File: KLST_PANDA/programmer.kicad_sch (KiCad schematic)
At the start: 8 parts, among them J1 ARM_JTAG_SWD(STDC14), J1 TC2070-IDC-NL

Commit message: started spec'ing components
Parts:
- J1: JLCPCB (none) -> DNF; JLCPCB Part # DNF -> (none)
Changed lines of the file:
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@@
       (effects (font (size 1.27 1.27)) hide)
     )
-    (property "JLCPCB Part #" "DNF" (at 31.75 46.99 0)
+    (property "JLCPCB Part #" "" (at 31.75 46.99 0)
+      (effects (font (size 1.27 1.27)) hide)
+    )
+    (property "JLCPCB" "DNF" (at 31.75 46.99 0)
       (effects (font (size 1.27 1.27)) hide)
     )
@@
       (effects (font (size 1.27 1.27)) hide)
     )
-    (property "JLCPCB Part #" "DNF" (at 100.965 46.99 0)
+    (property "JLCPCB Part #" "" (at 100.965 46.99 0)
       (effects (font (size 1.27 1.27)) hide)
     )
+    (property "JLCPCB" "DNF" (at 100.965 46.99 0)
+      (effects (font (size 1.27 1.27)) hide)
+    )

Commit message: assigned footprints
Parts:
- R53, R54, R55, R56, R57, R58: footprint (none) -> Resistor_SMD:R_0402_1005Metric; JLCPCB (none) -> C114765
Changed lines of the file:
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@@
       (effects (font (size 1.27 1.27)))
     )
-    (property "Footprint" "" (at 191.135 36.83 0)
+    (property "Footprint" "Resistor_SMD:R_0402_1005Metric" (at 191.135 36.83 0)
       (effects (font (size 1.27 1.27)) hide)
     )
     (property "Datasheet" "~" (at 191.135 36.83 0)
+      (effects (font (size 1.27 1.27)) hide)
+    )
+    (property "Description" "62.5mW" (at 191.135 36.83 0)
+      (effects (font (size 1.27 1.27)) hide)
+    )
+    (property "JLCPCB" "C114765" (at 191.135 36.83 0)
       (effects (font (size 1.27 1.27)) hide)
     )
@@
       (effects (font (size 1.27 1.27)))
     )
-    (property "Footprint" "" (at 191.135 55.88 0)
+    (property "Footprint" "Resistor_SMD:R_0402_1005Metric" (at 191.135 55.88 0)
       (effects (font (size 1.27 1.27)) hide)
     )
     (property "Datasheet" "~" (at 191.135 55.88 0)
+      (effects (font (size 1.27 1.27)) hide)
+    )
+    (property "Description" "62.5mW" (at 191.135 55.88 0)
+      (effects (font (size 1.27 1.27)) hide)
+    )
+    (property "JLCPCB" "C114765" (at 191.135 55.88 0)
       (effects (font (size 1.27 1.27)) hide)
     )
@@
       (effects (font (size 1.27 1.27)))
     )
-    (property "Footprint" "" (at 191.135 43.18 0)
+    (property "Footprint" "Resistor_SMD:R_0402_1005Metric" (at 191.135 43.18 0)
       (effects (font (size 1.27 1.27)) hide)
     )
@@
       (effects (font (size 1.27 1.27)) hide)
     )
+    (property "Description" "62.5mW" (at 191.135 43.18 0)
+      (effects (font (size 1.27 1.27)) hide)
+    )
+    (property "JLCPCB" "C114765" (at 191.135 43.18 0)
+      (effects (font (size 1.27 1.27)) hide)
+    )
     (pin "1")
     (pin "2")
@@
       (effects (font (size 1.27 1.27)))
     )
-    (property "Footprint" "" (at 191.135 49.53 0)
+    (property "Footprint" "Resistor_SMD:R_0402_1005Metric" (at 191.135 49.53 0)
       (effects (font (size 1.27 1.27)) hide)
     )
     (property "Datasheet" "~" (at 191.135 49.53 0)
+      (effects (font (size 1.27 1.27)) hide)
+    )
+    (property "Description" "62.5mW" (at 191.135 49.53 0)
+      (effects (font (size 1.27 1.27)) hide)
+    )
+    (property "JLCPCB" "C114765" (at 191.135 49.53 0)
       (effects (font (size 1.27 1.27)) hide)
     )
@@
       (effects (font (size 1.27 1.27)))
     )
-    (property "Footprint" "" (at 191.135 62.23 0)
+    (property "Footprint" "Resistor_SMD:R_0402_1005Metric" (at 191.135 62.23 0)
       (effects (font (size 1.27 1.27)) hide)
     )
     (property "Datasheet" "~" (at 191.135 62.23 0)
+      (effects (font (size 1.27 1.27)) hide)
+    )
+    (property "Description" "62.5mW" (at 191.135 62.23 0)
+      (effects (font (size 1.27 1.27)) hide)
+    )
+    (property "JLCPCB" "C114765" (at 191.135 62.23 0)
       (effects (font (size 1.27 1.27)) hide)
     )
@@
       (effects (font (size 1.27 1.27)))
     )
-    (property "Footprint" "" (at 191.135 30.48 0)
+    (property "Footprint" "Resistor_SMD:R_0402_1005Metric" (at 191.135 30.48 0)
       (effects (font (size 1.27 1.27)) hide)
     )
@@
       (effects (font (size 1.27 1.27)) hide)
     )
+    (property "Description" "62.5mW" (at 191.135 30.48 0)
+      (effects (font (size 1.27 1.27)) hide)
+    )
+    (property "JLCPCB" "C114765" (at 191.135 30.48 0)
+      (effects (font (size 1.27 1.27)) hide)
+    )

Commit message: cleaned up footprint assignment
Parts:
- J1: MFR.Part # DNF -> (none)
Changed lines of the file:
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@@
-      (effects (font (size 1.27 1.27)) hide)
-    )
-    (property "LCSC Part #" "" (at 31.75 46.99 0)
-      (effects (font (size 1.27 1.27)) hide)
-    )
-    (property "MFR.Part #" "DNF" (at 31.75 46.99 0)
-      (effects (font (size 1.27 1.27)) hide)
-    )
-    (property "JLCPCB Part #" "" (at 31.75 46.99 0)
       (effects (font (size 1.27 1.27)) hide)
     )
@@
       (effects (font (size 1.27 1.27)) hide)
     )
-    (property "LCSC Part #" "" (at 100.965 46.99 0)
-      (effects (font (size 1.27 1.27)) hide)
-    )
-    (property "MFR.Part #" "DNF" (at 100.965 46.99 0)
-      (effects (font (size 1.27 1.27)) hide)
-    )
-    (property "JLCPCB Part #" "" (at 100.965 46.99 0)
-      (effects (font (size 1.27 1.27)) hide)
-    )

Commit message: routed some components
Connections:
- net NRST: no longer J1.12 (~{RST}), J1.12 (~{RST}), R53.1
- new net RST: J1.12 (~{RST}), J1.12 (~{RST}), R53.1
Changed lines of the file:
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@@
     (effects (font (size 1.27 1.27)) (justify left bottom))
   )
-  (label "NRST" (at 44.45 34.29 0) (fields_autoplaced)
+  (label "RST" (at 44.45 34.29 0) (fields_autoplaced)
     (effects (font (size 1.27 1.27)) (justify left bottom))
   )
@@
     (effects (font (size 1.27 1.27)) (justify left bottom))
   )
+  (label "RST" (at 186.055 30.48 180) (fields_autoplaced)
+    (effects (font (size 1.27 1.27)) (justify right bottom))
+  )
   (label "SWD_OUT" (at 113.665 44.45 0) (fields_autoplaced)
     (effects (font (size 1.27 1.27)) (justify left bottom))
   )
-  (label "NRST" (at 186.055 30.48 180) (fields_autoplaced)
-    (effects (font (size 1.27 1.27)) (justify right bottom))
+  (label "SERIAL_TX" (at 113.665 59.69 0) (fields_autoplaced)
+    (effects (font (size 1.27 1.27)) (justify left bottom))
   )
-  (label "SERIAL_TX" (at 113.665 59.69 0) (fields_autoplaced)
+  (label "RST" (at 113.665 34.29 0) (fields_autoplaced)
     (effects (font (size 1.27 1.27)) (justify left bottom))
   )
@@
     (effects (font (size 1.27 1.27)) (justify right bottom))
   )
-  (label "NRST" (at 113.665 34.29 0) (fields_autoplaced)
-    (effects (font (size 1.27 1.27)) (justify left bottom))
-  )
   (label "SWD_CLK" (at 44.45 39.37 0) (fields_autoplaced)

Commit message: added ( maybe fit ) Samtec FTSH-107-01-F-DV-K for programmer
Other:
- note added: "@TODO( maybe fit Samtec FTSH-107-01-F-DV-K for assembly )"
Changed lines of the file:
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@@
+    (effects (font (size 1.27 1.27)) (justify left bottom))
+  )
+  (text "@TODO( maybe fit Samtec FTSH-107-01-F-DV-K for assembly )"
+    (at 15.875 78.105 0)
     (effects (font (size 1.27 1.27)) (justify left bottom))
   )

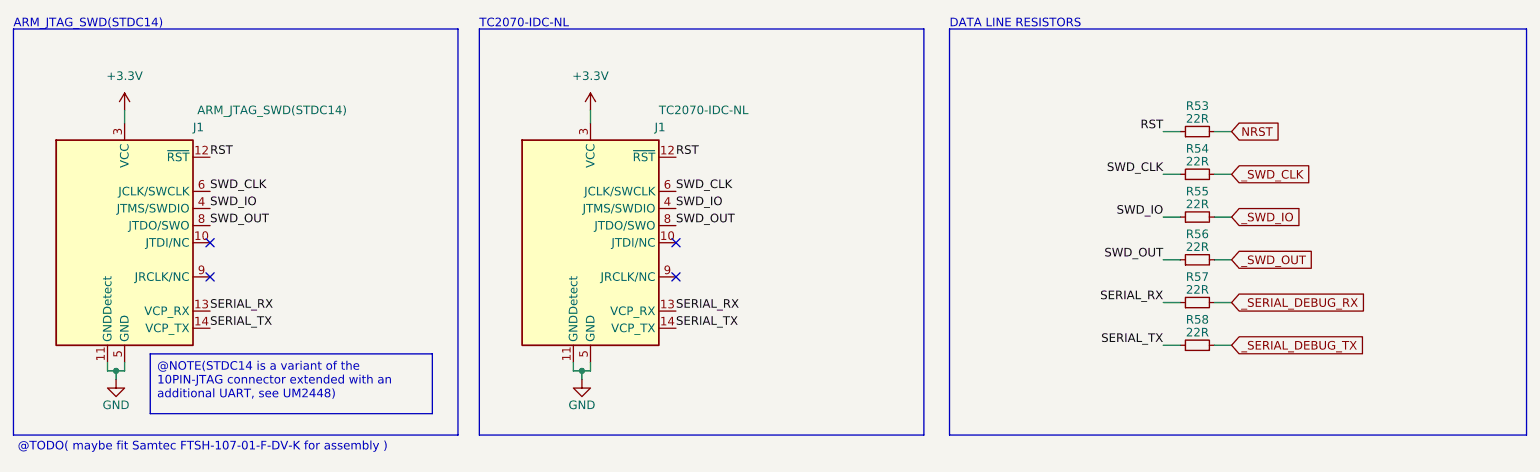
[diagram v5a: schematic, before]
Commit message: added resistor and capacitor, cleaned up TODOs
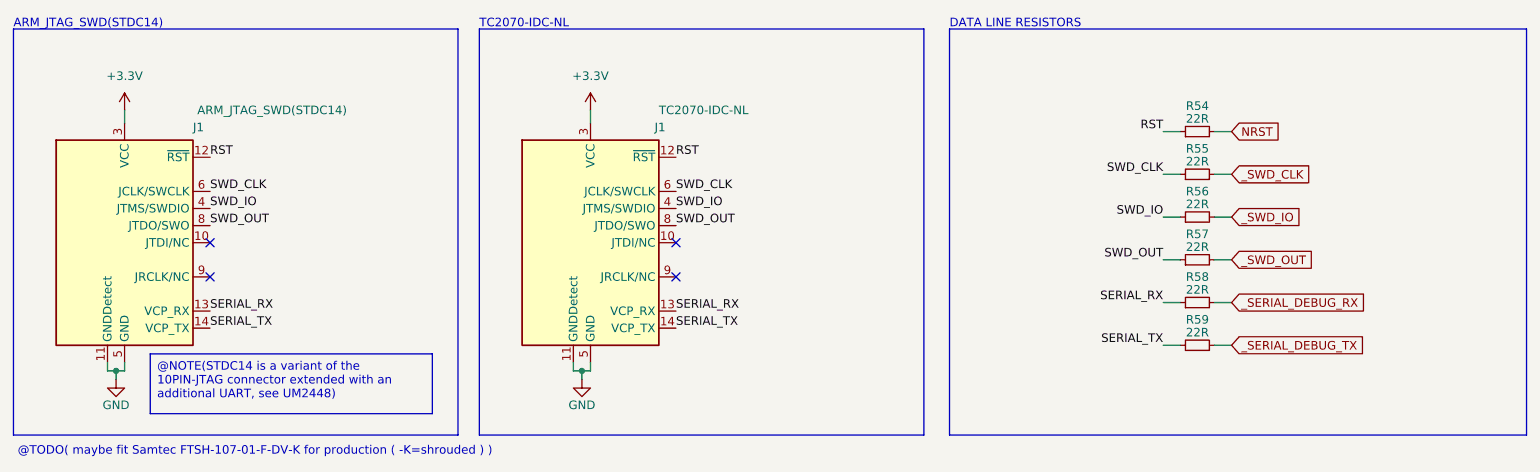
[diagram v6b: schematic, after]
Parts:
- J1: JLCPCB DNF -> C2881912
- renumbered R53 to R54, R54 to R55, R55 to R56, R56 to R57, R57 to R58, R58 to R59
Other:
- note added: "@TODO( maybe fit Samtec FTSH-107-01-F-DV-K for production ( -K=shrouded ) )"
- note removed: "@TODO( maybe fit Samtec FTSH-107-01-F-DV-K for assembly )"
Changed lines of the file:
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@@
     (effects (font (size 1.27 1.27)) (justify left bottom))
   )
-  (text "@TODO( maybe fit Samtec FTSH-107-01-F-DV-K for assembly )"
-    (at 15.875 78.105 0)
+  (text "@TODO( maybe fit Samtec FTSH-107-01-F-DV-K for production ( -K=shrouded ) )"
+    (at 15.875 78.74 0)
     (effects (font (size 1.27 1.27)) (justify left bottom))
   )
@@
   (symbol (lib_id "Device:R_Small") (at 191.135 36.83 90) (unit 1)
     (in_bom yes) (on_board yes) (dnp no)
-    (property "Reference" "R54" (at 191.135 33.02 90)
+    (property "Reference" "R55" (at 191.135 33.02 90)
       (effects (font (size 1.27 1.27)))
     )
@@
       (project "KLST_PANDA"
         (path "/b4513875-4c57-4720-bcc5-43ead67fe18f/2ad43130-8b99-4527-817e-e6414020b242"
-          (reference "R54") (unit 1)
+          (reference "R55") (unit 1)
         )
       )
@@
         )
         (path "/b4513875-4c57-4720-bcc5-43ead67fe18f/2ad43130-8b99-4527-817e-e6414020b242"
-          (reference "#PWR086") (unit 1)
+          (reference "#PWR088") (unit 1)
         )
       )
@@
   (symbol (lib_id "Device:R_Small") (at 191.135 55.88 90) (unit 1)
     (in_bom yes) (on_board yes) (dnp no)
-    (property "Reference" "R57" (at 191.135 52.07 90)
+    (property "Reference" "R58" (at 191.135 52.07 90)
       (effects (font (size 1.27 1.27)))
     )
@@
       (project "KLST_PANDA"
         (path "/b4513875-4c57-4720-bcc5-43ead67fe18f/2ad43130-8b99-4527-817e-e6414020b242"
-          (reference "R57") (unit 1)
+          (reference "R58") (unit 1)
         )
       )
@@
       (effects (font (size 1.27 1.27)) hide)
     )
-    (property "JLCPCB" "DNF" (at 31.75 46.99 0)
+    (property "JLCPCB" "C2881912" (at 31.75 46.99 0)
       (effects (font (size 1.27 1.27)) hide)
     )
@@
         )
         (path "/b4513875-4c57-4720-bcc5-43ead67fe18f/2ad43130-8b99-4527-817e-e6414020b242"
-          (reference "#PWR087") (unit 1)
+          (reference "#PWR089") (unit 1)
         )
       )
@@
   (symbol (lib_id "Device:R_Small") (at 191.135 43.18 90) (unit 1)
     (in_bom yes) (on_board yes) (dnp no)
-    (property "Reference" "R55" (at 191.135 39.37 90)
+    (property "Reference" "R56" (at 191.135 39.37 90)
       (effects (font (size 1.27 1.27)))
     )
@@
       (project "KLST_PANDA"
         (path "/b4513875-4c57-4720-bcc5-43ead67fe18f/2ad43130-8b99-4527-817e-e6414020b242"
-          (reference "R55") (unit 1)
+          (reference "R56") (unit 1)
         )
       )
@@
   (symbol (lib_id "Device:R_Small") (at 191.135 49.53 90) (unit 1)
     (in_bom yes) (on_board yes) (dnp no)
-    (property "Reference" "R56" (at 191.135 45.72 90)
+    (property "Reference" "R57" (at 191.135 45.72 90)
       (effects (font (size 1.27 1.27)))
     )
@@
       (project "KLST_PANDA"
         (path "/b4513875-4c57-4720-bcc5-43ead67fe18f/2ad43130-8b99-4527-817e-e6414020b242"
-          (reference "R56") (unit 1)
+          (reference "R57") (unit 1)
         )
       )
@@
         )
         (path "/b4513875-4c57-4720-bcc5-43ead67fe18f/2ad43130-8b99-4527-817e-e6414020b242"
-          (reference "#PWR085") (unit 1)
+          (reference "#PWR087") (unit 1)
         )
       )
@@
   (symbol (lib_id "Device:R_Small") (at 191.135 62.23 90) (unit 1)
     (in_bom yes) (on_board yes) (dnp no)
-    (property "Reference" "R58" (at 191.135 58.42 90)
+    (property "Reference" "R59" (at 191.135 58.42 90)
       (effects (font (size 1.27 1.27)))
     )
@@
       (project "KLST_PANDA"
         (path "/b4513875-4c57-4720-bcc5-43ead67fe18f/2ad43130-8b99-4527-817e-e6414020b242"
-          (reference "R58") (unit 1)
+          (reference "R59") (unit 1)
         )
       )
@@
   (symbol (lib_id "Device:R_Small") (at 191.135 30.48 90) (unit 1)
     (in_bom yes) (on_board yes) (dnp no)
-    (property "Reference" "R53" (at 191.135 26.67 90)
+    (property "Reference" "R54" (at 191.135 26.67 90)
       (effects (font (size 1.27 1.27)))
     )
@@
       (project "KLST_PANDA"
         (path "/b4513875-4c57-4720-bcc5-43ead67fe18f/2ad43130-8b99-4527-817e-e6414020b242"
-          (reference "R53") (unit 1)
+          (reference "R54") (unit 1)
         )
       )
@@
         )
         (path "/b4513875-4c57-4720-bcc5-43ead67fe18f/2ad43130-8b99-4527-817e-e6414020b242"
-          (reference "#PWR084") (unit 1)
-        )
-      )
+          (reference "#PWR086") (unit 1)
+        )
+      )

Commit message: started updating PCB
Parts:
- renumbered J1 to J14, J1 to J15
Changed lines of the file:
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@@
   (symbol (lib_id "power:GND") (at 99.695 67.31 0) (unit 1)
     (in_bom yes) (on_board yes) (dnp no)
-    (property "Reference" "#PWR025" (at 99.695 73.66 0)
+    (property "Reference" "#PWR088" (at 99.695 73.66 0)
       (effects (font (size 1.27 1.27)) hide)
     )
@@
     (instances
       (project "KLST_PANDA"
-        (path "/b4513875-4c57-4720-bcc5-43ead67fe18f"
-          (reference "#PWR025") (unit 1)
-        )
         (path "/b4513875-4c57-4720-bcc5-43ead67fe18f/2ad43130-8b99-4527-817e-e6414020b242"
           (reference "#PWR088") (unit 1)
@@
   (symbol (lib_id "Connector:Conn_ST_STDC14") (at 31.75 46.99 0) (unit 1)
     (in_bom yes) (on_board yes) (dnp no)
-    (property "Reference" "J1" (at 41.91 29.845 0)
+    (property "Reference" "J14" (at 41.91 29.845 0)
       (effects (font (size 1.27 1.27)) (justify left))
     )
@@
     (instances
       (project "KLST_PANDA"
-        (path "/b4513875-4c57-4720-bcc5-43ead67fe18f"
-          (reference "J1") (unit 1)
-        )
         (path "/b4513875-4c57-4720-bcc5-43ead67fe18f/2ad43130-8b99-4527-817e-e6414020b242"
           (reference "J14") (unit 1)
@@
   (symbol (lib_id "power:+3.3V") (at 100.965 27.305 0) (unit 1)
     (in_bom yes) (on_board yes) (dnp no) (fields_autoplaced)
-    (property "Reference" "#PWR077" (at 100.965 31.115 0)
+    (property "Reference" "#PWR089" (at 100.965 31.115 0)
       (effects (font (size 1.27 1.27)) hide)
     )
@@
     (instances
       (project "KLST_PANDA"
-        (path "/b4513875-4c57-4720-bcc5-43ead67fe18f/47e8e77e-c64e-4c44-bfd8-2073580a3d85"
-          (reference "#PWR077") (unit 1)
-        )
         (path "/b4513875-4c57-4720-bcc5-43ead67fe18f/2ad43130-8b99-4527-817e-e6414020b242"
           (reference "#PWR089") (unit 1)
@@
   (symbol (lib_id "power:+3.3V") (at 31.75 27.305 0) (unit 1)
     (in_bom yes) (on_board yes) (dnp no) (fields_autoplaced)
-    (property "Reference" "#PWR077" (at 31.75 31.115 0)
+    (property "Reference" "#PWR087" (at 31.75 31.115 0)
       (effects (font (size 1.27 1.27)) hide)
     )
@@
     (instances
       (project "KLST_PANDA"
-        (path "/b4513875-4c57-4720-bcc5-43ead67fe18f/47e8e77e-c64e-4c44-bfd8-2073580a3d85"
-          (reference "#PWR077") (unit 1)
-        )
         (path "/b4513875-4c57-4720-bcc5-43ead67fe18f/2ad43130-8b99-4527-817e-e6414020b242"
           (reference "#PWR087") (unit 1)
@@
   (symbol (lib_id "Connector:Conn_ST_STDC14") (at 100.965 46.99 0) (unit 1)
     (in_bom no) (on_board yes) (dnp no)
-    (property "Reference" "J1" (at 110.49 29.845 0)
+    (property "Reference" "J15" (at 110.49 29.845 0)
       (effects (font (size 1.27 1.27)) (justify left))
     )
@@
     (instances
       (project "KLST_PANDA"
-        (path "/b4513875-4c57-4720-bcc5-43ead67fe18f"
-          (reference "J1") (unit 1)
-        )
         (path "/b4513875-4c57-4720-bcc5-43ead67fe18f/2ad43130-8b99-4527-817e-e6414020b242"
           (reference "J15") (unit 1)
@@
   (symbol (lib_id "power:GND") (at 30.48 67.31 0) (unit 1)
     (in_bom yes) (on_board yes) (dnp no)
-    (property "Reference" "#PWR025" (at 30.48 73.66 0)
+    (property "Reference" "#PWR086" (at 30.48 73.66 0)
       (effects (font (size 1.27 1.27)) hide)
     )
@@
     (instances
       (project "KLST_PANDA"
-        (path "/b4513875-4c57-4720-bcc5-43ead67fe18f"
-          (reference "#PWR025") (unit 1)
-        )
         (path "/b4513875-4c57-4720-bcc5-43ead67fe18f/2ad43130-8b99-4527-817e-e6414020b242"
           (reference "#PWR086") (unit 1)
